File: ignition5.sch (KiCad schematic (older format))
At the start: 9 parts, among them P8 CONN_1, P9 CONN_1, Q2 MOSFET_N, SW2 SWITCH_INV

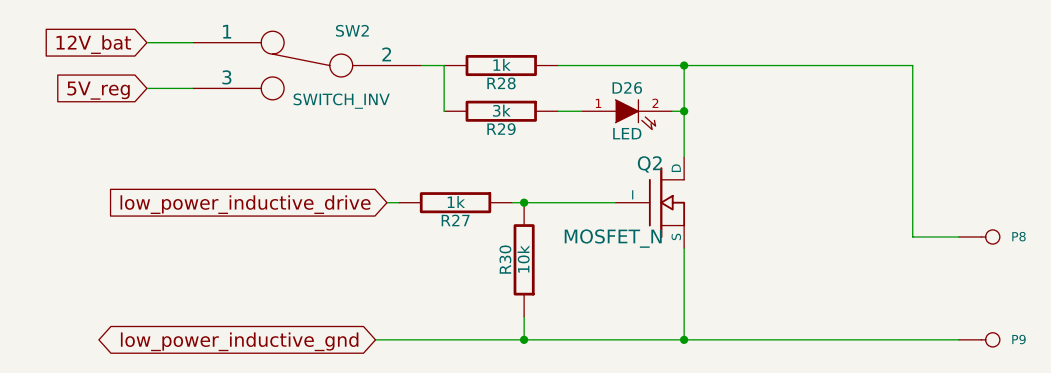
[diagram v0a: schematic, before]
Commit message: Removed LM1815 options. Now adaptive mode and square waves are the default,
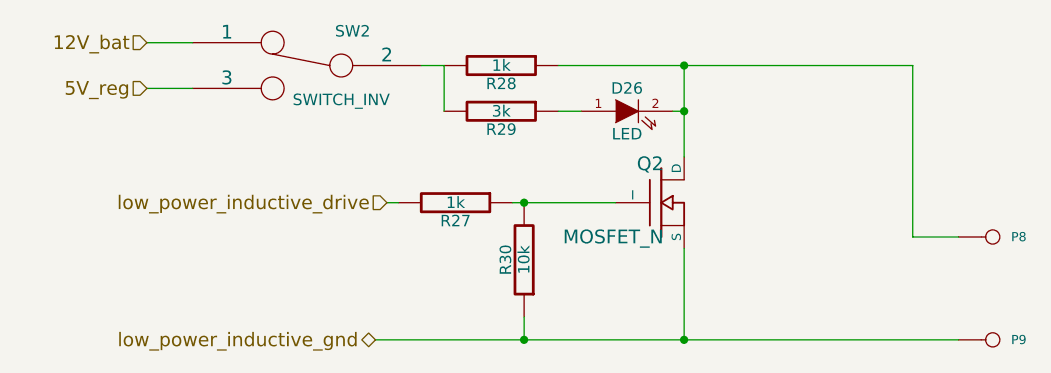
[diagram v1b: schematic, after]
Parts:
- D26: Field1 (none) -> newark,58k2469; Field2 (none) -> vendor1, smd w hem; Field3 (none) -> vendor2, thru w hem; Field4 (none) -> vendor2, smd w hem; Field5 (none) -> x,x; Field6 (none) -> x,x; Field7 (none) -> green; Field8 (none) -> other,more,stuff
- Q2: Field1 (none) -> digi,PIP3104-ND; Field2 (none) -> vendor1, smd w hem; Field3 (none) -> vendor2, thru w hem; Field4 (none) -> vendor2, smd w hem; Field5 (none) -> 8,A; Field6 (none) -> x,x; Field7 (none) -> TOPFET; Field8 (none) -> other,more,stuff
- R27, R28: Field1 (none) -> newark,38k0327; Field2 (none) -> vendor1, smd w hem; Field3 (none) -> vendor2, thru w hem; Field4 (none) -> vendor2, smd w hem; Field5 (none) -> 250,mW; Field6 (none) -> 5,%; Field7 (none) -> carbon film; Field8 (none) -> other,more,stuff
- R29: Field1 (none) -> newark,38k0340; Field2 (none) -> vendor1, smd w hem; Field3 (none) -> vendor2, thru w hem; Field4 (none) -> vendor2, smd w hem; Field5 (none) -> 1/4,W; Field6 (none) -> 5,%; Field7 (none) -> carbon film; Field8 (none) -> other,more,stuff
- R30: Field1 (none) -> newark,38k0328; Field2 (none) -> vendor1, smd w hem; Field3 (none) -> vendor2, thru w hem; Field4 (none) -> vendor2, smd w hem; Field5 (none) -> 250,mW; Field6 (none) -> 5,%; Field7 (none) -> carbon film; Field8 (none) -> other,more,stuff
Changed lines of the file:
@@
-EESchema Schematic File Version 1
-LIBS:power,./freeEMS_lib,device,conn,linear,regul,74xx,cmos4000,adc-dac,memory,xilinx,special,microcontrollers,dsp,microchip,analog_switches,motorola,texas,intel,audio,interface,digital-audio,philips,display,cypress,siliconi,contrib,valves,./freeEMS_1.cache
+EESchema Schematic File Version 2  date Fri 02 Jul 2010 02:24:35 PM ART
+LIBS:power
+LIBS:freeEMS_lib
+LIBS:device
+LIBS:conn
+LIBS:linear
+LIBS:regul
+LIBS:74xx
+LIBS:cmos4000
+LIBS:adc-dac
+LIBS:memory
+LIBS:xilinx
+LIBS:special
+LIBS:microcontrollers
+LIBS:dsp
+LIBS:microchip
+LIBS:analog_switches
+LIBS:motorola
+LIBS:texas
+LIBS:intel
+LIBS:audio
+LIBS:interface
+LIBS:digital-audio
+LIBS:philips
+LIBS:display
+LIBS:cypress
+LIBS:siliconi
+LIBS:contrib
+LIBS:valves
+LIBS:freeEMS_1-cache
 EELAYER 23  0
 EELAYER END
@@
 Sheet 11 41
 Title "freeEMS 1.0"
-Date "15 nov 2008"
+Date "2 jul 2010"
 Rev "A.20"
 Comp "diyefi.org"
@@
 U 1 1 48B16ED5
 P 4000 2050
-F 0 "Q2" H 4010 2220 60  0000 R C
-F 1 "MOSFET_N" H 4010 1900 60  0000 R C
-F 2 "TO220_sm" V 3930 2800 60  0001 C C
-F 4 "digi,PIP3104-ND" V 2130 3800 60  0001 C C
-F 5 "vendor1, smd w hem" V 2130 3800 60  0001 C C
-F 6 "vendor2, thru w hem" V 2130 3800 60  0001 C C
-F 7 "vendor2, smd w hem" V 2130 3800 60  0001 C C
-F 8 "8,A" V 2130 3800 60  0001 C C
-F 9 "x,x" V 2130 3800 60  0001 C C
-F 10 "TOPFET" V 2130 3800 60  0001 C C
-F 11 "other,more,stuff" V 2130 3800 60  0001 C C
+F 0 "Q2" H 4010 2220 60  0000 R CNN
+F 1 "MOSFET_N" H 4010 1900 60  0000 R CNN
+F 2 "TO220_sm" V 3930 2800 60  0001 C CNN
+F 4 "digi,PIP3104-ND" V 2130 3800 60  0001 C CNN "Field1"
+F 5 "vendor1, smd w hem" V 2130 3800 60  0001 C CNN "Field2"
+F 6 "vendor2, thru w hem" V 2130 3800 60  0001 C CNN "Field3"
+F 7 "vendor2, smd w hem" V 2130 3800 60  0001 C CNN "Field4"
+F 8 "8,A" V 2130 3800 60  0001 C CNN "Field5"
+F 9 "x,x" V 2130 3800 60  0001 C CNN "Field6"
+F 10 "TOPFET" V 2130 3800 60  0001 C CNN "Field7"
+F 11 "other,more,stuff" V 2130 3800 60  0001 C CNN "Field8"
 	1    4000 2050
 	1    0    0    -1
@@
 U 1 1 48AE08BB
 P 3400 2300
-F 0 "R30" V 3480 2300 50  0000 C C
-F 1 "10k" V 3400 2300 50  0000 C C
-F 2 "R4-SM0805" V 3580 2400 60  0001 C C
-F 4 "newark,38k0328" V 1230 2850 60  0001 C C
-F 5 "vendor1, smd w hem" V 1230 2850 60  0001 C C
-F 6 "vendor2, thru w hem" V 1230 2850 60  0001 C C
-F 7 "vendor2, smd w hem" V 1230 2850 60  0001 C C
-F 8 "250,mW" V 1230 2850 60  0001 C C
-F 9 "5,%" V 1230 2850 60  0001 C C
-F 10 "carbon film" V 1230 2850 60  0001 C C
-F 11 "other,more,stuff" V 1230 2850 60  0001 C C
+F 0 "R30" V 3480 2300 50  0000 C CNN
+F 1 "10k" V 3400 2300 50  0000 C CNN
+F 2 "R4-SM0805" V 3580 2400 60  0001 C CNN
+F 4 "newark,38k0328" V 1230 2850 60  0001 C CNN "Field1"
+F 5 "vendor1, smd w hem" V 1230 2850 60  0001 C CNN "Field2"
+F 6 "vendor2, thru w hem" V 1230 2850 60  0001 C CNN "Field3"
+F 7 "vendor2, smd w hem" V 1230 2850 60  0001 C CNN "Field4"
+F 8 "250,mW" V 1230 2850 60  0001 C CNN "Field5"
+F 9 "5,%" V 1230 2850 60  0001 C CNN "Field6"
+F 10 "carbon film" V 1230 2850 60  0001 C CNN "Field7"
+F 11 "other,more,stuff" V 1230 2850 60  0001 C CNN "Field8"
 	1    3400 2300
 	-1   0    0    1
@@
 U 1 1 48AE0832
 P 2450 1450
-F 0 "SW2" H 2250 1600 50  0000 C C
-F 1 "SWITCH_INV" H 2300 1300 50  0000 C C
-F 2 "SIL-3" H 2350 1700 60  0001 C C
+F 0 "SW2" H 2250 1600 50  0000 C CNN
+F 1 "SWITCH_INV" H 2300 1300 50  0000 C CNN
+F 2 "SIL-3" H 2350 1700 60  0001 C CNN
 	1    2450 1450
 	-1   0    0    -1
@@
 U 1 1 48AA2529
 P 3850 1650
-F 0 "D26" H 3850 1750 50  0000 C C
-F 1 "LED" H 3850 1550 50  0000 C C
-F 2 "LEDV" V 1680 5050 60  0001 C C
-F 4 "newark,58k2469" V 430 2100 60  0001 C C
-F 5 "vendor1, smd w hem" V 430 2100 60  0001 C C
-F 6 "vendor2, thru w hem" V 430 2100 60  0001 C C
-F 7 "vendor2, smd w hem" V 430 2100 60  0001 C C
-F 8 "x,x" V 430 2100 60  0001 C C
-F 9 "x,x" V 430 2100 60  0001 C C
-F 10 "green" V 430 2100 60  0001 C C
-F 11 "other,more,stuff" V 430 2100 60  0001 C C
+F 0 "D26" H 3850 1750 50  0000 C CNN
+F 1 "LED" H 3850 1550 50  0000 C CNN
+F 2 "LEDV" V 1680 5050 60  0001 C CNN
+F 4 "newark,58k2469" V 430 2100 60  0001 C CNN "Field1"
+F 5 "vendor1, smd w hem" V 430 2100 60  0001 C CNN "Field2"
+F 6 "vendor2, thru w hem" V 430 2100 60  0001 C CNN "Field3"
+F 7 "vendor2, smd w hem" V 430 2100 60  0001 C CNN "Field4"
+F 8 "x,x" V 430 2100 60  0001 C CNN "Field5"
+F 9 "x,x" V 430 2100 60  0001 C CNN "Field6"
+F 10 "green" V 430 2100 60  0001 C CNN "Field7"
+F 11 "other,more,stuff" V 430 2100 60  0001 C CNN "Field8"
 	1    3850 1650
 	1    0    0    -1
@@
 U 1 1 48AA2523
 P 3300 1650
-F 0 "R29" V 3380 1650 50  0000 C C
-F 1 "3k" V 3300 1650 50  0000 C C
-F 2 "R4-SM0805" V 1980 1650 60  0001 C C
-F 4 "newark,38k0340" V -120 2400 60  0001 C C
-F 5 "vendor1, smd w hem" V -120 2400 60  0001 C C
-F 6 "vendor2, thru w hem" V -120 2400 60  0001 C C
-F 7 "vendor2, smd w hem" V -120 2400 60  0001 C C
-F 8 "1/4,W" V -120 2400 60  0001 C C
-F 9 "5,%" V -120 2400 60  0001 C C
-F 10 "carbon film" V -120 2400 60  0001 C C
-F 11 "other,more,stuff" V -120 2400 60  0001 C C
+F 0 "R29" V 3380 1650 50  0000 C CNN
+F 1 "3k" V 3300 1650 50  0000 C CNN
+F 2 "R4-SM0805" V 1980 1650 60  0001 C CNN
+F 4 "newark,38k0340" V -120 2400 60  0001 C CNN "Field1"
+F 5 "vendor1, smd w hem" V -120 2400 60  0001 C CNN "Field2"
+F 6 "vendor2, thru w hem" V -120 2400 60  0001 C CNN "Field3"
+F 7 "vendor2, smd w hem" V -120 2400 60  0001 C CNN "Field4"
+F 8 "1/4,W" V -120 2400 60  0001 C CNN "Field5"
+F 9 "5,%" V -120 2400 60  0001 C CNN "Field6"
+F 10 "carbon film" V -120 2400 60  0001 C CNN "Field7"
+F 11 "other,more,stuff" V -120 2400 60  0001 C CNN "Field8"
 	1    3300 1650
 	0    1    1    0
@@
 U 1 1 48AA1A4E
 P 5450 2650
-F 0 "P9" H 5530 2650 40  0000 L C
-F 1 "CONN_1" H 5450 2705 30  0001 C C
-F 2 "1PIN" V 1880 2850 60  0001 C C
+F 0 "P9" H 5530 2650 40  0000 L CNN
+F 1 "CONN_1" H 5450 2705 30  0001 C CNN
+F 2 "1PIN" V 1880 2850 60  0001 C CNN
 	1    5450 2650
 	1    0    0    -1
@@
 U 1 1 48AA1A4A
 P 5450 2200
-F 0 "P8" H 5530 2200 40  0000 L C
-F 1 "CONN_1" H 5450 2255 30  0001 C C
-F 2 "1PIN" V 1880 2600 60  0001 C C
+F 0 "P8" H 5530 2200 40  0000 L CNN
+F 1 "CONN_1" H 5450 2255 30  0001 C CNN
+F 2 "1PIN" V 1880 2600 60  0001 C CNN
 	1    5450 2200
 	1    0    0    -1
 $EndComp
-Text GLabel 1750 1550 0    60   Input
+Text HLabel 1750 1550 0    60   Input ~ 0
 5V_reg
 $Comp
@@
 U 1 1 489395E6
 P 3100 2050
-F 0 "R27" V 3180 2050 50  0000 C C
-F 1 "1k" V 3100 2050 50  0000 C C
-F 2 "R4-SM0805" V 3280 2150 60  0001 C C
-F 4 "newark,38k0327" V 930 2600 60  0001 C C
-F 5 "vendor1, smd w hem" V 930 2600 60  0001 C C
-F 6 "vendor2, thru w hem" V 930 2600 60  0001 C C
-F 7 "vendor2, smd w hem" V 930 2600 60  0001 C C
-F 8 "250,mW" V 930 2600 60  0001 C C
-F 9 "5,%" V 930 2600 60  0001 C C
-F 10 "carbon film" V 930 2600 60  0001 C C
-F 11 "other,more,stuff" V 930 2600 60  0001 C C
+F 0 "R27" V 3180 2050 50  0000 C CNN
+F 1 "1k" V 3100 2050 50  0000 C CNN
+F 2 "R4-SM0805" V 3280 2150 60  0001 C CNN
+F 4 "newark,38k0327" V 930 2600 60  0001 C CNN "Field1"
+F 5 "vendor1, smd w hem" V 930 2600 60  0001 C CNN "Field2"
+F 6 "vendor2, thru w hem" V 930 2600 60  0001 C CNN "Field3"
+F 7 "vendor2, smd w hem" V 930 2600 60  0001 C CNN "Field4"
+F 8 "250,mW" V 930 2600 60  0001 C CNN "Field5"
+F 9 "5,%" V 930 2600 60  0001 C CNN "Field6"
+F 10 "carbon film" V 930 2600 60  0001 C CNN "Field7"
+F 11 "other,more,stuff" V 930 2600 60  0001 C CNN "Field8"
 	1    3100 2050
 	0    1    1    0
@@
 U 1 1 489395D4
 P 3300 1450
-F 0 "R28" V 3380 1450 50  0000 C C
-F 1 "1k" V 3300 1450 50  0000 C C
-F 2 "R4-SM0805" V 3480 1550 60  0001 C C
-F 4 "newark,38k0327" V 1130 2350 60  0001 C C
-F 5 "vendor1, smd w hem" V 1130 2350 60  0001 C C
-F 6 "vendor2, thru w hem" V 1130 2350 60  0001 C C
-F 7 "vendor2, smd w hem" V 1130 2350 60  0001 C C
-F 8 "250,mW" V 1130 2350 60  0001 C C
-F 9 "5,%" V 1130 2350 60  0001 C C
-F 10 "carbon film" V 1130 2350 60  0001 C C
-F 11 "other,more,stuff" V 1130 2350 60  0001 C C
+F 0 "R28" V 3380 1450 50  0000 C CNN
+F 1 "1k" V 3300 1450 50  0000 C CNN
+F 2 "R4-SM0805" V 3480 1550 60  0001 C CNN
+F 4 "newark,38k0327" V 1130 2350 60  0001 C CNN "Field1"
+F 5 "vendor1, smd w hem" V 1130 2350 60  0001 C CNN "Field2"
+F 6 "vendor2, thru w hem" V 1130 2350 60  0001 C CNN "Field3"
+F 7 "vendor2, smd w hem" V 1130 2350 60  0001 C CNN "Field4"
+F 8 "250,mW" V 1130 2350 60  0001 C CNN "Field5"
+F 9 "5,%" V 1130 2350 60  0001 C CNN "Field6"
+F 10 "carbon film" V 1130 2350 60  0001 C CNN "Field7"
+F 11 "other,more,stuff" V 1130 2350 60  0001 C CNN "Field8"
 	1    3300 1450
 	0    1    1    0
 $EndComp
-Text GLabel 1750 1350 0    60   Input
+Text HLabel 1750 1350 0    60   Input ~ 0
 12V_bat
-Text GLabel 2750 2650 0    60   BiDi
+Text HLabel 2750 2650 0    60   BiDi ~ 0
 low_power_inductive_gnd
-Text GLabel 2800 2050 0    60   Input
+Text HLabel 2800 2050 0    60   Input ~ 0
 low_power_inductive_drive
 $EndSCHEMATC

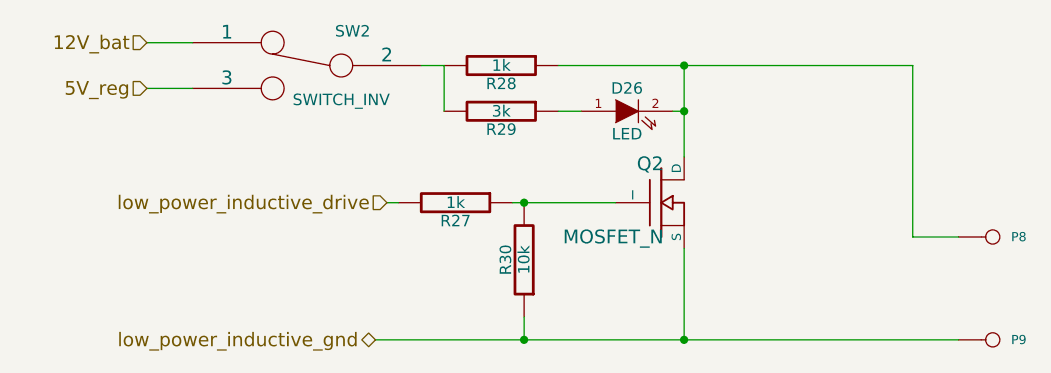
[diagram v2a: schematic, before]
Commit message: Implemented P&H, removed current sense circuitry, removed all unnecessary files from the repo
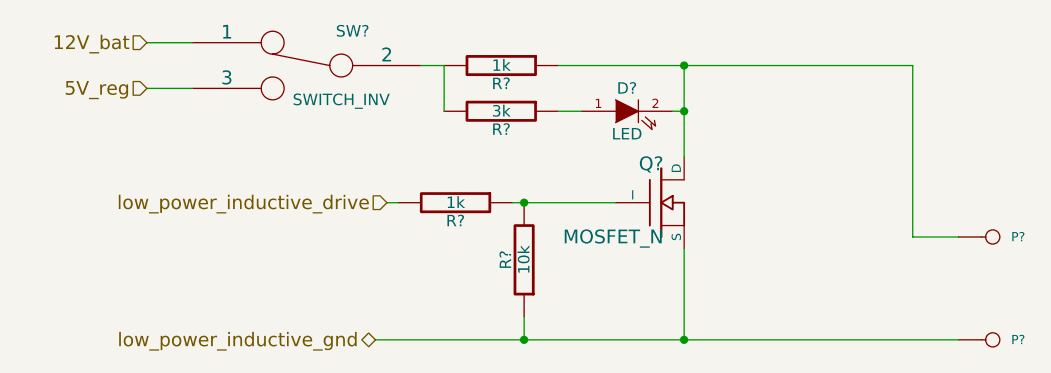
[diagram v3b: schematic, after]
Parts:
- R?: renamed from R30; Field1 newark,38k0328 -> newark,38K0328
- renumbered D26 to D?, P8 to P?, P9 to P?, Q2 to Q?, R28 to R?, R27 to R?, R29 to R?, SW2 to SW?
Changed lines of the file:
@@
-EESchema Schematic File Version 2  date Fri 02 Jul 2010 05:44:26 PM ART
+EESchema Schematic File Version 2  date Sat 03 Jul 2010 10:49:02 AM ART
 LIBS:power
 LIBS:freeEMS_lib
@@
 EELAYER END
 $Descr A4 11700 8267
-Sheet 11 41
+Sheet 1 41
 Title "freeEMS 1.0"
-Date "2 jul 2010"
-Rev "A.20"
+Date "3 jul 2010"
+Rev "A.07"
 Comp "diyefi.org"
 Comment1 "ignition.sch"
@@
 Connection ~ 3400 2050
 $Comp
-L PIP-3104 Q2
+L PIP-3104 Q?
 U 1 1 48B16ED5
 P 4000 2050
-F 0 "Q2" H 4010 2220 60  0000 R CNN
+F 0 "Q?" H 4010 2220 60  0000 R CNN
 F 1 "MOSFET_N" H 4010 1900 60  0000 R CNN
 F 2 "TO220_sm" V 3930 2800 60  0001 C CNN
@@
 $EndComp
 $Comp
-L R R30
+L R R?
 U 1 1 48AE08BB
 P 3400 2300
-F 0 "R30" V 3480 2300 50  0000 C CNN
+F 0 "R?" V 3480 2300 50  0000 C CNN
 F 1 "10k" V 3400 2300 50  0000 C CNN
 F 2 "R4-SM0805" V 3580 2400 60  0001 C CNN
-F 4 "newark,38k0328" V 1230 2850 60  0001 C CNN "Field1"
+F 4 "newark,38K0328" V 1230 2850 60  0001 C CNN "Field1"
 F 5 "vendor1, smd w hem" V 1230 2850 60  0001 C CNN "Field2"
 F 6 "vendor2, thru w hem" V 1230 2850 60  0001 C CNN "Field3"
@@
 $EndComp
 $Comp
-L SWITCH_INV SW2
+L SWITCH_INV SW?
 U 1 1 48AE0832
 P 2450 1450
-F 0 "SW2" H 2250 1600 50  0000 C CNN
+F 0 "SW?" H 2250 1600 50  0000 C CNN
 F 1 "SWITCH_INV" H 2300 1300 50  0000 C CNN
 F 2 "SIL-3" H 2350 1700 60  0001 C CNN
@@
 $EndComp
 $Comp
-L LED D26
+L LED D?
 U 1 1 48AA2529
 P 3850 1650
-F 0 "D26" H 3850 1750 50  0000 C CNN
+F 0 "D?" H 3850 1750 50  0000 C CNN
 F 1 "LED" H 3850 1550 50  0000 C CNN
 F 2 "LEDV" V 1680 5050 60  0001 C CNN
@@
 $EndComp
 $Comp
-L R R29
+L R R?
 U 1 1 48AA2523
 P 3300 1650
-F 0 "R29" V 3380 1650 50  0000 C CNN
+F 0 "R?" V 3380 1650 50  0000 C CNN
 F 1 "3k" V 3300 1650 50  0000 C CNN
 F 2 "R4-SM0805" V 1980 1650 60  0001 C CNN
@@
 $EndComp
 $Comp
-L CONN_1 P9
+L CONN_1 P?
 U 1 1 48AA1A4E
 P 5450 2650
-F 0 "P9" H 5530 2650 40  0000 L CNN
+F 0 "P?" H 5530 2650 40  0000 L CNN
 F 1 "CONN_1" H 5450 2705 30  0001 C CNN
 F 2 "1PIN" V 1880 2850 60  0001 C CNN
@@
 $EndComp
 $Comp
-L CONN_1 P8
+L CONN_1 P?
 U 1 1 48AA1A4A
 P 5450 2200
-F 0 "P8" H 5530 2200 40  0000 L CNN
+F 0 "P?" H 5530 2200 40  0000 L CNN
 F 1 "CONN_1" H 5450 2255 30  0001 C CNN
 F 2 "1PIN" V 1880 2600 60  0001 C CNN
@@
 5V_reg
 $Comp
-L R R27
+L R R?
 U 1 1 489395E6
 P 3100 2050
-F 0 "R27" V 3180 2050 50  0000 C CNN
+F 0 "R?" V 3180 2050 50  0000 C CNN
 F 1 "1k" V 3100 2050 50  0000 C CNN
 F 2 "R4-SM0805" V 3280 2150 60  0001 C CNN
@@
 $EndComp
 $Comp
-L R R28
+L R R?
 U 1 1 489395D4
 P 3300 1450
-F 0 "R28" V 3380 1450 50  0000 C CNN
+F 0 "R?" V 3380 1450 50  0000 C CNN
 F 1 "1k" V 3300 1450 50  0000 C CNN
 F 2 "R4-SM0805" V 3480 1550 60  0001 C CNN

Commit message: Corrected ERC errors by fixing the custom FreeEMS components pinouts
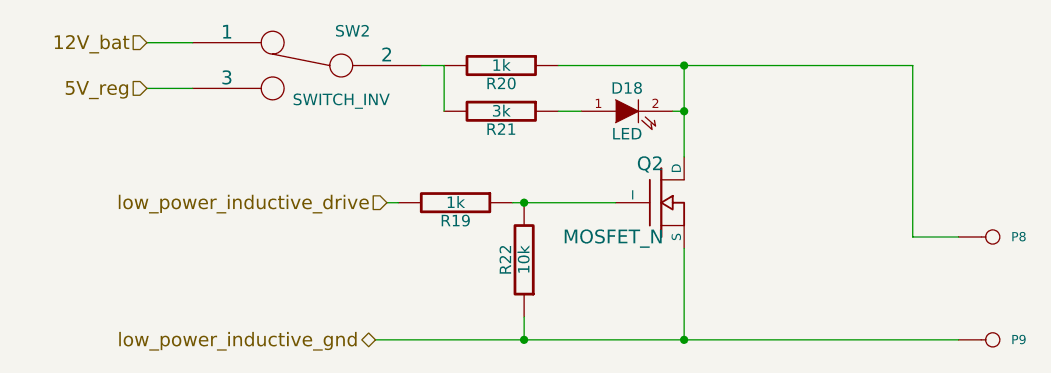
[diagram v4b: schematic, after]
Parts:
- removed D?: LED, LEDV, symbol LED
- removed P? (x2): CONN_1, 1PIN, symbol CONN_1
- removed Q?: MOSFET_N, TO220_sm, symbol PIP-3104
- removed R? (x2): 1k, R4-SM0805, symbol R
- removed R?: 3k, R4-SM0805, symbol R
- removed R?: 10k, R4-SM0805, symbol R
- removed SW?: SWITCH_INV, SIL-3, symbol SWITCH_INV
- added D18: LED, LEDV, symbol LED
- added P8, P9: CONN_1, 1PIN, symbol CONN_1
- added Q2: MOSFET_N, TO220_sm, symbol PIP-3104
- added R19, R20: 1k, R4-SM0805, symbol R
- added R21: 3k, R4-SM0805, symbol R
- added R22: 10k, R4-SM0805, symbol R
- added SW2: SWITCH_INV, SIL-3, symbol SWITCH_INV
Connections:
- net 12V_bat: now also SW2.1
- net 5V_reg: now also SW2.3
- net low_power_inductive_drive: now also R19.2
- net low_power_inductive_gnd: now also P9.1, Q2.3 (S), R22.1
- new net: D18.2 (K), P8.1, Q2.2 (D), R20.1
- new net: R20.2, R21.2, SW2.2
- new net: Q2.1 (I), R19.1, R22.2
- new net: D18.1 (A), R21.1
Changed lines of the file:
@@
-EESchema Schematic File Version 2  date Sat 03 Jul 2010 10:49:02 AM ART
+EESchema Schematic File Version 2  date Sat 03 Jul 2010 12:32:24 PM ART
 LIBS:power
 LIBS:freeEMS_lib
@@
 EELAYER END
 $Descr A4 11700 8267
-Sheet 1 41
+Sheet 17 41
 Title "freeEMS 1.0"
 Date "3 jul 2010"
@@
 Connection ~ 3400 2050
 $Comp
-L PIP-3104 Q?
-U 1 1 48B16ED5
+L PIP-3104 Q2
+U 1 1 4C2F5336
 P 4000 2050
-F 0 "Q?" H 4010 2220 60  0000 R CNN
+F 0 "Q2" H 4010 2220 60  0000 R CNN
 F 1 "MOSFET_N" H 4010 1900 60  0000 R CNN
 F 2 "TO220_sm" V 3930 2800 60  0001 C CNN
@@
 $EndComp
 $Comp
-L R R?
-U 1 1 48AE08BB
+L R R22
+U 1 1 4C2F532A
 P 3400 2300
-F 0 "R?" V 3480 2300 50  0000 C CNN
+F 0 "R22" V 3480 2300 50  0000 C CNN
 F 1 "10k" V 3400 2300 50  0000 C CNN
 F 2 "R4-SM0805" V 3580 2400 60  0001 C CNN
@@
 $EndComp
 $Comp
-L SWITCH_INV SW?
-U 1 1 48AE0832
+L SWITCH_INV SW2
+U 1 1 4C2F5324
 P 2450 1450
-F 0 "SW?" H 2250 1600 50  0000 C CNN
+F 0 "SW2" H 2250 1600 50  0000 C CNN
 F 1 "SWITCH_INV" H 2300 1300 50  0000 C CNN
 F 2 "SIL-3" H 2350 1700 60  0001 C CNN
@@
 $EndComp
 $Comp
-L LED D?
-U 1 1 48AA2529
+L LED D18
+U 1 1 4C2F531F
 P 3850 1650
-F 0 "D?" H 3850 1750 50  0000 C CNN
+F 0 "D18" H 3850 1750 50  0000 C CNN
 F 1 "LED" H 3850 1550 50  0000 C CNN
 F 2 "LEDV" V 1680 5050 60  0001 C CNN
@@
 $EndComp
 $Comp
-L R R?
-U 1 1 48AA2523
+L R R21
+U 1 1 4C2F531A
 P 3300 1650
-F 0 "R?" V 3380 1650 50  0000 C CNN
+F 0 "R21" V 3380 1650 50  0000 C CNN
 F 1 "3k" V 3300 1650 50  0000 C CNN
 F 2 "R4-SM0805" V 1980 1650 60  0001 C CNN
@@
 $EndComp
 $Comp
-L CONN_1 P?
-U 1 1 48AA1A4E
+L CONN_1 P9
+U 1 1 4C2F5313
 P 5450 2650
-F 0 "P?" H 5530 2650 40  0000 L CNN
+F 0 "P9" H 5530 2650 40  0000 L CNN
 F 1 "CONN_1" H 5450 2705 30  0001 C CNN
 F 2 "1PIN" V 1880 2850 60  0001 C CNN
@@
 $EndComp
 $Comp
-L CONN_1 P?
-U 1 1 48AA1A4A
+L CONN_1 P8
+U 1 1 4C2F530F
 P 5450 2200
-F 0 "P?" H 5530 2200 40  0000 L CNN
+F 0 "P8" H 5530 2200 40  0000 L CNN
 F 1 "CONN_1" H 5450 2255 30  0001 C CNN
 F 2 "1PIN" V 1880 2600 60  0001 C CNN
@@
 5V_reg
 $Comp
-L R R?
-U 1 1 489395E6
+L R R19
+U 1 1 4C2F52E9
 P 3100 2050
-F 0 "R?" V 3180 2050 50  0000 C CNN
+F 0 "R19" V 3180 2050 50  0000 C CNN
 F 1 "1k" V 3100 2050 50  0000 C CNN
 F 2 "R4-SM0805" V 3280 2150 60  0001 C CNN
@@
 $EndComp
 $Comp
-L R R?
-U 1 1 489395D4
+L R R20
+U 1 1 4C2F52E3
 P 3300 1450
-F 0 "R?" V 3380 1450 50  0000 C CNN
+F 0 "R20" V 3380 1450 50  0000 C CNN
 F 1 "1k" V 3300 1450 50  0000 C CNN
 F 2 "R4-SM0805" V 3480 1550 60  0001 C CNN
